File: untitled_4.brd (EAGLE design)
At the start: 100 x 93.2 mm, 75 parts, among them IC1 LM1875T, IC2 LM1875T, IC3 LM1875T, IC4 LM1875T, J2 power, J3 audio_output, J5 +25v, J6 audio_output, K1 12v, K2 12v

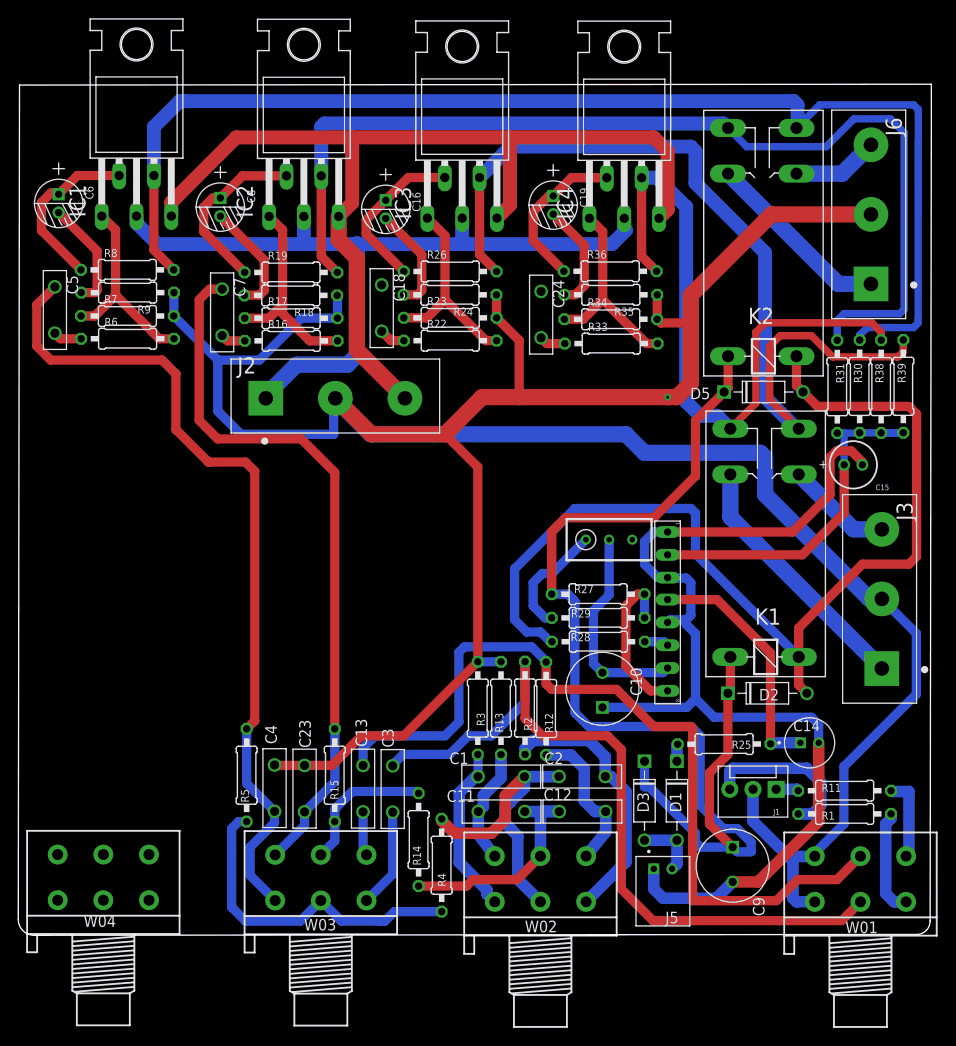
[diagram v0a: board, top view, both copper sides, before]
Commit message: 后级放大:更新
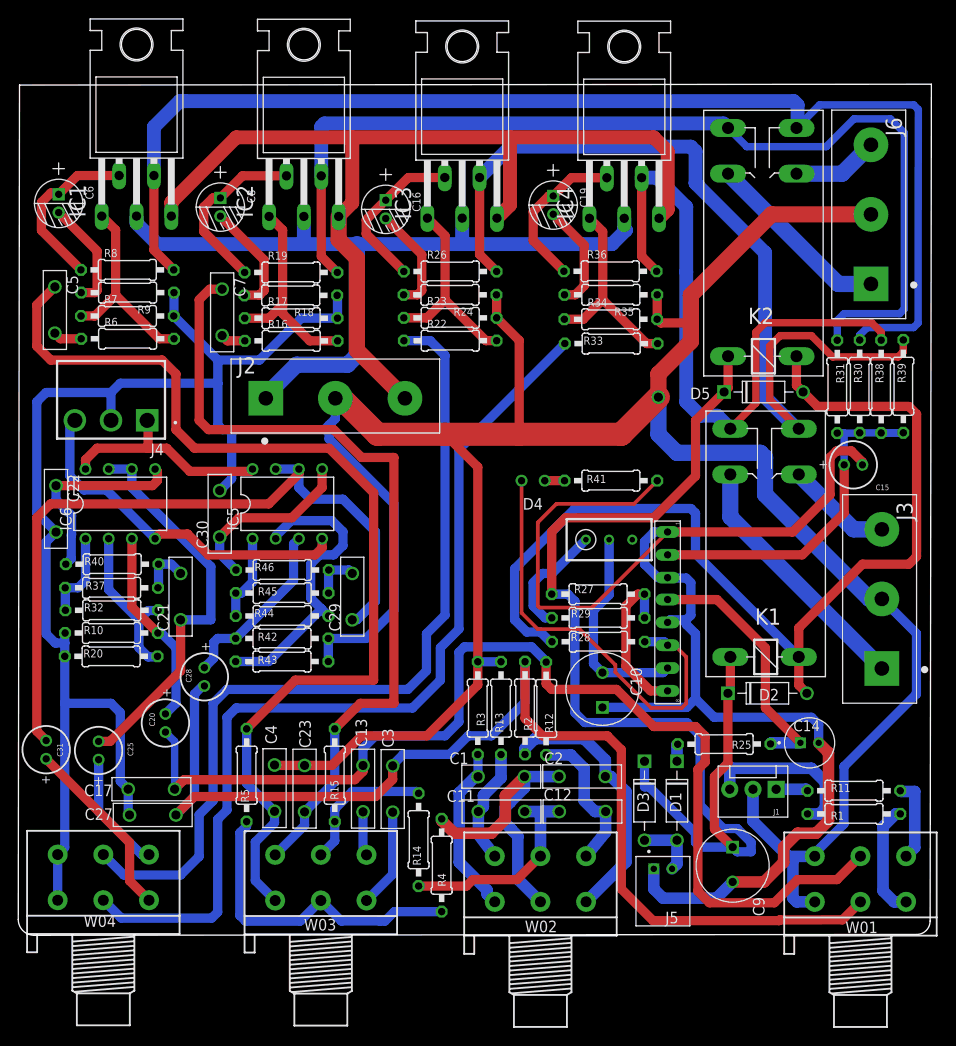
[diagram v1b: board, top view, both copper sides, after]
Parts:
- removed C18, C24: 2u2, Audio-Power-amlifier:5.08MM-独石电容
- added C17, C22, C27, C30: 104, Audio-Power-amlifier:5.08MM-独石电容
- added C20, C25, C28, C31: 10µF/50v, Wurth_Capacitors_WCAP-AT1H:WCAP-AT1H_5X11(DXL)
- added C21, C29: 0.22, Audio-Power-amlifier:5.08MM-独石电容
- added D4: (no value), BeagleBone_Blue_R3:BEAGLEBONE_BLUE_BEAGLEBONE_BLUE_LED3MM-NS
- added IC5, IC6: NE5532N, linear:DIL08
- added J4: B3P-VH(LF)(SN), Connectors:HDR-03
- added R10, R42: 47k, OPL_Resistor:PR-D2.3XL6.5MM
- added R20, R43: 5k, OPL_Resistor:PR-D2.3XL6.5MM
- added R32, R44: 33k, OPL_Resistor:PR-D2.3XL6.5MM
- added R37, R40, R41, R45, R46: 10k, OPL_Resistor:PR-D2.3XL6.5MM
- moved R1 1.02 mm to (91.4, 13.3)
- moved R11 1.02 mm to (91.4, 15.8)
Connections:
- removed net N$53: C24.P$2, R33.1
- new net N$27: C20.1, IC6.3, R10.2
- new net N$39: IC6.2, R20.2, R32.2
- new net N$55: IC6.1, R32.1, R37.2
- new net N$58: C13.P$1, C17.P$2, C20.2, R12.1, W01.2-2
- new net N$59: C21.P$2, R37.1, R40.2
- new net N$60: C22.P$1, IC6.5, R40.1
- new net N$61: C21.P$1, C25.2, IC6.6, IC6.7
- new net N$62: C29.P$1, C31.2, IC5.6, IC5.7
- new net N$63: IC5.2, R43.2, R44.2
- new net N$64: IC5.1, R44.1, R45.2
- new net N$65: C29.P$2, R45.1, R46.2
- new net N$66: C30.P$1, IC5.5, R46.1
- new net N$68: C31.1, W04.1-3
- new net N$69: C25.1, W04.2-3
- new net V+: IC5.8, IC6.8, J4.1
- new net V-: IC5.4, IC6.4, J4.3
- net GND: now also C17.P$1, C22.P$2, C27.P$1, C30.P$2, J4.2, R10.1, R20.1, R42.1, R43.1, W04.1-1, W04.2-1
- net N$16: now also C27.P$2, C28.2, C3.P$1, R2.1, W01.1-2; no longer C13.P$1, R12.1, W01.2-2
- net N$2: now also D4.K, R41.2; no longer C3.P$1, R2.1, W01.1-2
- net N$33: now also R33.1, W04.1-2; no longer C18.P$1
- net N$37: now also W04.2-2; no longer C18.P$2
- net N$41: now also D4.A
- net N$49: now also C28.1, IC5.3, R42.2; no longer C24.P$1
- net N$56: now also R41.1
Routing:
- net N$58: track 0.00 -> 120.4 mm
- net GND: track 326.2 -> 439.3 mm
- net N$33: track 0.00 -> 102.9 mm
- net N$37: track 2.85 -> 95.1 mm
- net N$62: track 0.00 -> 82.0 mm
- net N$2: track 83.8 -> 2.16 mm
- net N$41: track 2.66 -> 47.8 mm
- net N$56: track 115.1 -> 159.4 mm
- net N$61: track 0.00 -> 43.7 mm
- net V-: track 0.00 -> 39.3 mm
- net N$16: track 91.5 -> 126.2 mm
- net N$63: track 0.00 -> 33.0 mm
- net V+: track 0.00 -> 24.1 mm
- net N$60: track 0.00 -> 22.3 mm
- net N$27: track 0.00 -> 21.9 mm
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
